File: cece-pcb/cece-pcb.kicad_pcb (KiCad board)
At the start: 2 copper layers, 64 x 90 mm, 52 parts, among them J1 SERIAL, J2 HTU21D, J3 Li-Ion Battery, J4 VAC, K1 SANYOU_SRD_Form_C, Q1 Q_NPN, Q2 Q_NPN, SW1 RES, U1 ESP-12F, U2 MCP73811T-420I-OT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

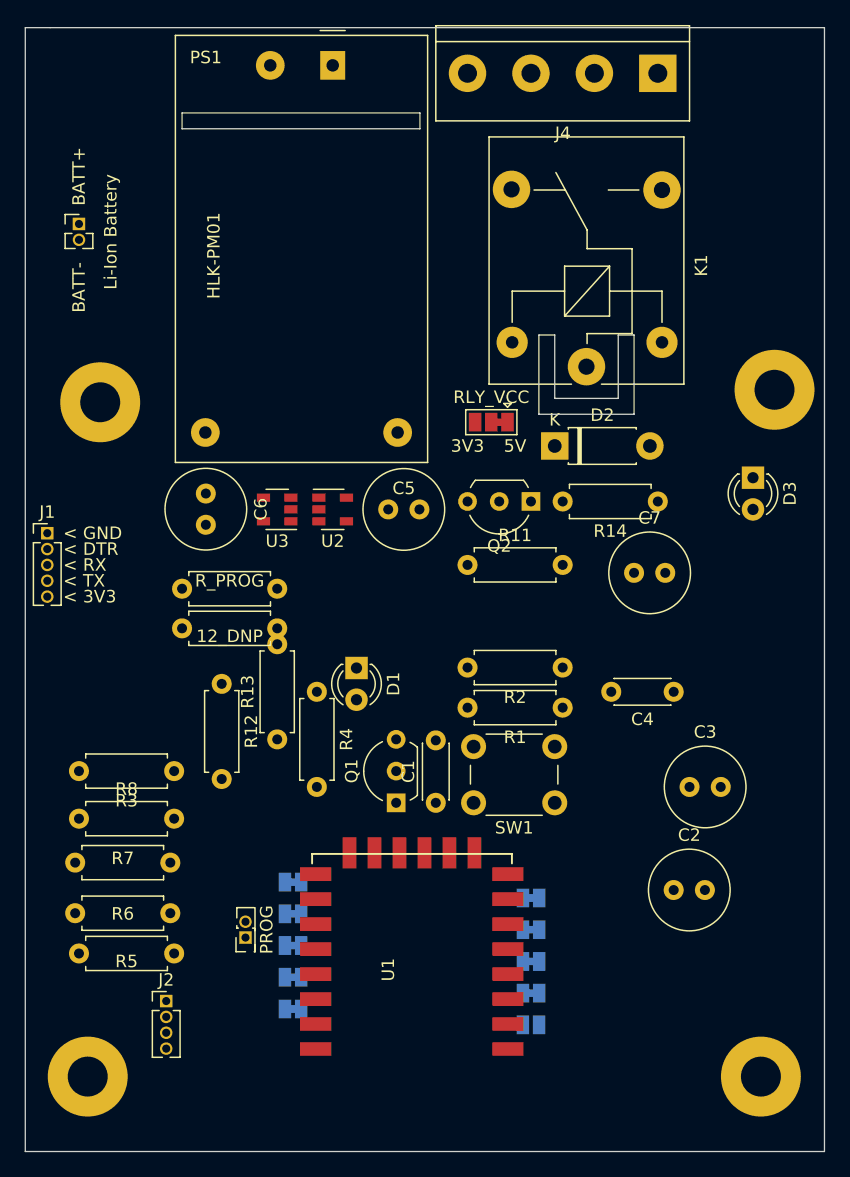
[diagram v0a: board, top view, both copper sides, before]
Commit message: Complete ESP-12 part of the PCB
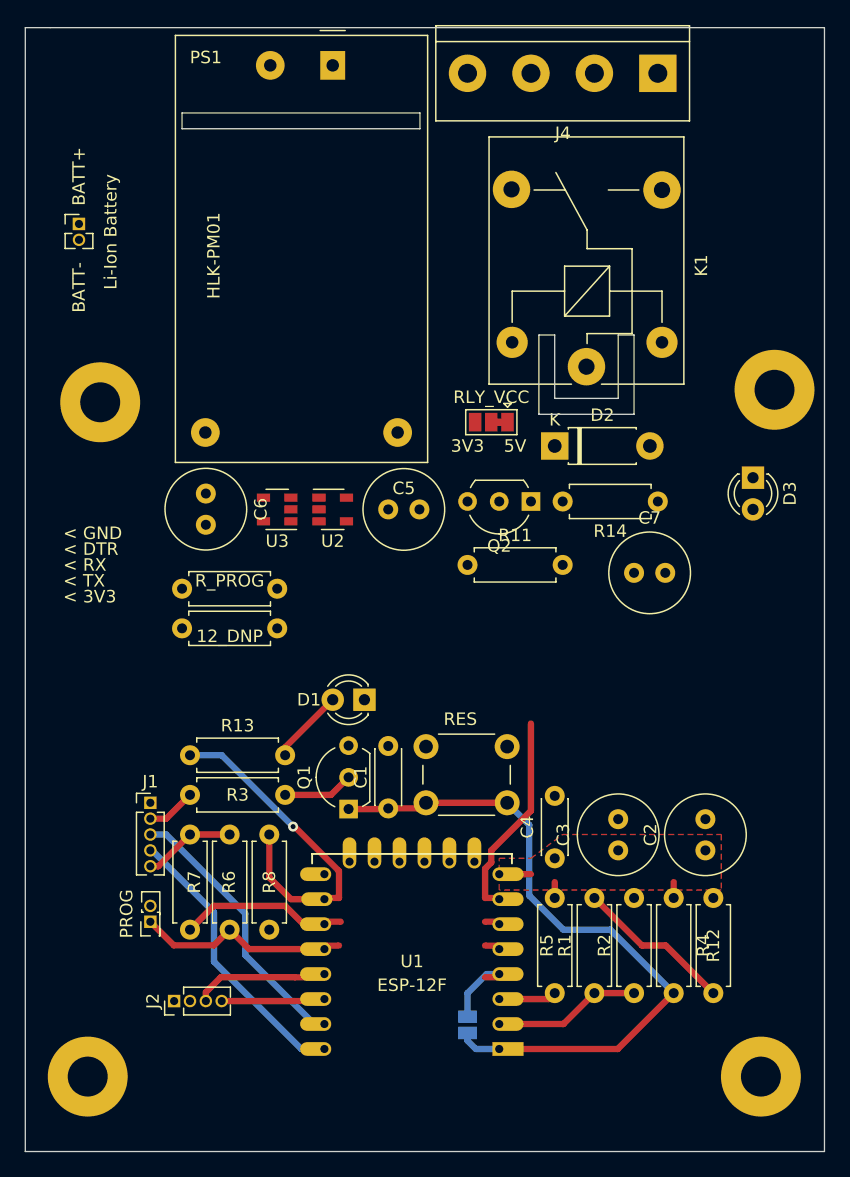
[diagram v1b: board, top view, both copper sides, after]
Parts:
- removed JP10: D4/GPIO2, Jumper:SolderJumper-2_P1.3mm_Bridged_Pad1.0x1.5mm
- removed JP2: D0/GPIO16, Jumper:SolderJumper-2_P1.3mm_Bridged_Pad1.0x1.5mm
- removed JP3: D5/GPIO14, Jumper:SolderJumper-2_P1.3mm_Bridged_Pad1.0x1.5mm
- removed JP4: D6/GPIO12, Jumper:SolderJumper-2_P1.3mm_Bridged_Pad1.0x1.5mm
- removed JP5: D7/GPIO13, Jumper:SolderJumper-2_P1.3mm_Bridged_Pad1.0x1.5mm
- removed JP6: D8/GPIO15, Jumper:SolderJumper-2_P1.3mm_Bridged_Pad1.0x1.5mm
- removed JP7: D1/GPIO5, Jumper:SolderJumper-2_P1.3mm_Bridged_Pad1.0x1.5mm
- removed JP8: D2/GPIO4, Jumper:SolderJumper-2_P1.3mm_Bridged_Pad1.0x1.5mm
- removed JP9: D3/GPIO0, Jumper:SolderJumper-2_P1.3mm_Bridged_Pad1.0x1.5mm
- added NT1: D0/GPIO16, NetTie:NetTie-2_SMD_Pad0.5mm, F.Cu at (147.3, 106.0)
- added NT2: D5/GPIO14, NetTie:NetTie-2_SMD_Pad0.5mm, F.Cu at (147.3, 103.5)
- added NT3: D6/GPIO12, NetTie:NetTie-2_SMD_Pad0.5mm, F.Cu at (147.3, 101.6)
- added NT4: D7/GPIO13, NetTie:NetTie-2_SMD_Pad0.5mm, F.Cu at (147.3, 99.7)
- added NT5: D8/GPIO15, NetTie:NetTie-2_SMD_Pad0.5mm, F.Cu at (134.6, 99.7)
- added NT6: D1/GPIO5, NetTie:NetTie-2_SMD_Pad0.5mm, F.Cu at (132.1, 108.0)
- added NT7: D2/GPIO4, NetTie:NetTie-2_SMD_Pad0.5mm, F.Cu at (132.1, 106.0)
- added NT8: D3/GPIO0, NetTie:NetTie-2_SMD_Pad0.5mm, F.Cu at (134.6, 103.5)
- added NT9: D4/GPIO2, NetTie:NetTie-2_SMD_Pad0.5mm, F.Cu at (134.8, 101.6)
- U1: footprint ESP8266:ESP-12E_SMD -> ESP8266:ESP-12E
- moved R12 46.5 mm to (165.1, 107.3), turned to 90 degrees
- moved R4 33.0 mm to (161.9, 99.7)
- moved R5 30.6 mm to (152.4, 107.3), turned to 90 degrees
- moved R2 26.7 mm to (158.8, 107.3), turned to 90 degrees
- moved J1 23.1 mm to (120.0, 92.1)
- moved R1 23.0 mm to (155.6, 107.3), turned to 90 degrees
- moved R8 17.6 mm to (129.5, 102.2), turned to 90 degrees
- moved C4 16.4 mm to (152.4, 96.5), turned to 90 degrees
- moved R3 9.09 mm to (130.8, 91.4)
- moved JP11 7.73 mm to (120.0, 101.6)
- moved C3 7.65 mm to (157.5, 95.9), turned to 90 degrees
- moved R13 7.10 mm to (123.2, 88.3), turned to 0 degrees
- moved R7 5.60 mm to (123.2, 102.2), turned to 90 degrees
- moved JP1 5.08 mm to (145.4, 109.9), turned to 90 degrees
- moved R6 4.93 mm to (126.4, 102.2), turned to 90 degrees
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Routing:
- net /ESP-12_common/RST: track 0.00 -> 55.1 mm
- net /TX: track 0.00 -> 22.8 mm
- net /RX: track 0.00 -> 22.2 mm
- net /ESP-12_common/D8: track 0.00 -> 18.0 mm, vias 0 -> 1
- net /ESP-12_common/GPIO0: track 0.00 -> 17.5 mm
- net /RLY: track 0.00 -> 15.5 mm
- net /ESP-12_common/A0: track 0.00 -> 12.7 mm
- net +3V3: track 0.00 -> 12.5 mm
- net /ESP-12_common/GPIO2: track 0.00 -> 12.2 mm
- net /ESP-12_common/ADC: track 0.00 -> 11.8 mm
- net /ESP-12_common/GPIO15: track 0.00 -> 10.2 mm
- net /HTU_SDA: track 0.00 -> 8.32 mm
- net Net-(D1-Pad2): track 0.00 -> 6.02 mm
- net /HTU_SCL: track 0.00 -> 5.82 mm
- net Net-(Q1-Pad2): track 0.00 -> 5.66 mm
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- added copper zone on F.Cu, net +3V3

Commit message: Finish first board revision
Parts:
- removed JP12: RLY_VCC, Jumper:SolderJumper-3_P1.3mm_Bridged12_Pad1.0x1.5mm
- removed R12: 100k, Resistor_THT:R_Axial_DIN0207_L6.3mm_D2.5mm_P7.62mm_Horizontal
- added JP2: VBATT_A0, Jumper:SolderJumper-2_P1.3mm_Bridged_Pad1.0x1.5mm, F.Cu at (161.8, 94.1)
- D3: footprint LED_THT:LED_D3.0mm -> LED_THT:LED_D5.0mm
- U2: moved to B.Cu
- moved J3 43.5 mm to (135.9, 83.5), turned to 270 degrees
- moved U3 25.6 mm to (150.4, 84.3), turned to 270 degrees
- moved C6 16.6 mm to (140.2, 72.6), turned to 180 degrees
- moved C5 15.6 mm to (124.0, 72.6)
- moved C7 15.4 mm to (146.1, 65.0), turned to 270 degrees
- moved C2 13.5 mm to (155.7, 85.6), turned to 0 degrees
- moved D3 12.1 mm to (161.0, 75.7), turned to 90 degrees
- moved R10 11.4 mm to (133.6, 77.7), turned to 90 degrees
- moved R11 9.71 mm to (154.2, 77.2), turned to 180 degrees
- moved H3 9.43 mm to (165.0, 67.0)
- moved D1 8.90 mm to (128.3, 84.3)
- moved H4 8.86 mm to (161.0, 110.0)
- moved J2 8.12 mm to (129.5, 105.2), turned to 0 degrees
- moved H2 8.06 mm to (122.0, 110.0)
- moved R9 8.01 mm to (130.6, 70.1), turned to 270 degrees
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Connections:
- C7 pad 1: Net-(C7-Pad1) -> +BATT
- D2 pad 1: Net-(C7-Pad1) -> +BATT
- J4 pad 1: /NC -> /NO
- J4 pad 2: /NO -> /NC
- K1 pad 5: Net-(C7-Pad1) -> +BATT
- NT1 pad 1: (no net) -> /ESP-12_common/D0
- NT2 pad 1: (no net) -> /ESP-12_common/D5|SCK
- NT3 pad 1: (no net) -> /ESP-12_common/D6|MISO
- NT8 pad 2: (no net) -> /ESP-12_common/D3
- NT9 pad 2: (no net) -> /ESP-12_common/D4
- R14 pad 2: Net-(C7-Pad1) -> +BATT
- U1 pad 17: (no net) -> Net-(U1-Pad17)
- U1 pad 18: (no net) -> Net-(U1-Pad18)
- U1 pad 19: (no net) -> Net-(U1-Pad19)
- U1 pad 20: (no net) -> Net-(U1-Pad20)
- U1 pad 21: (no net) -> Net-(U1-Pad21)
- U1 pad 22: (no net) -> Net-(U1-Pad22)
- U3 pad 4: (no net) -> Net-(U3-Pad4)
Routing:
- net +BATT: track 0.00 -> 82.4 mm
- net +3V3: track 12.5 -> 75.2 mm
- net /C: track 0.00 -> 55.4 mm
- net /RLY: track 15.5 -> 47.6 mm, vias 0 -> 2
- net Net-(D2-Pad2): track 0.00 -> 21.9 mm
- net +5V: track 0.00 -> 20.9 mm
- net /NC: track 0.00 -> 14.6 mm
- net /LN: track 0.00 -> 11.1 mm
- net /ESP-12_common/RST: track 55.1 -> 44.4 mm
- net /NO: track 0.00 -> 9.48 mm
- net /ESP-12_common/A0: track 12.7 -> 4.24 mm
- net Net-(R10-Pad1): track 0.00 -> 6.15 mm
- net /ESP-12_common/D8: track 18.0 -> 12.4 mm, vias 1 -> 2
- net /ESP-12_common/ADC: track 11.8 -> 17.4 mm
- net /HTU_SDA: track 8.32 -> 2.91 mm
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- added copper zone on B.Cu, net GND
- added copper zone on F.Cu, net GND
- removed copper zone on F.Cu, net +3V3
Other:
- board size 64 x 90 mm -> 57 x 86 mm
- board text added: "+"
- board text added: "<"
- board text removed: "3V3"
- board text removed: "5V"
- board text removed: "< 3V3"
- board text removed: "< DTR"
- board text removed: "< GND"
- board text removed: "< RX"
- board text removed: "< TX"
- board text removed: "BATT+"
- board text removed: "BATT-"

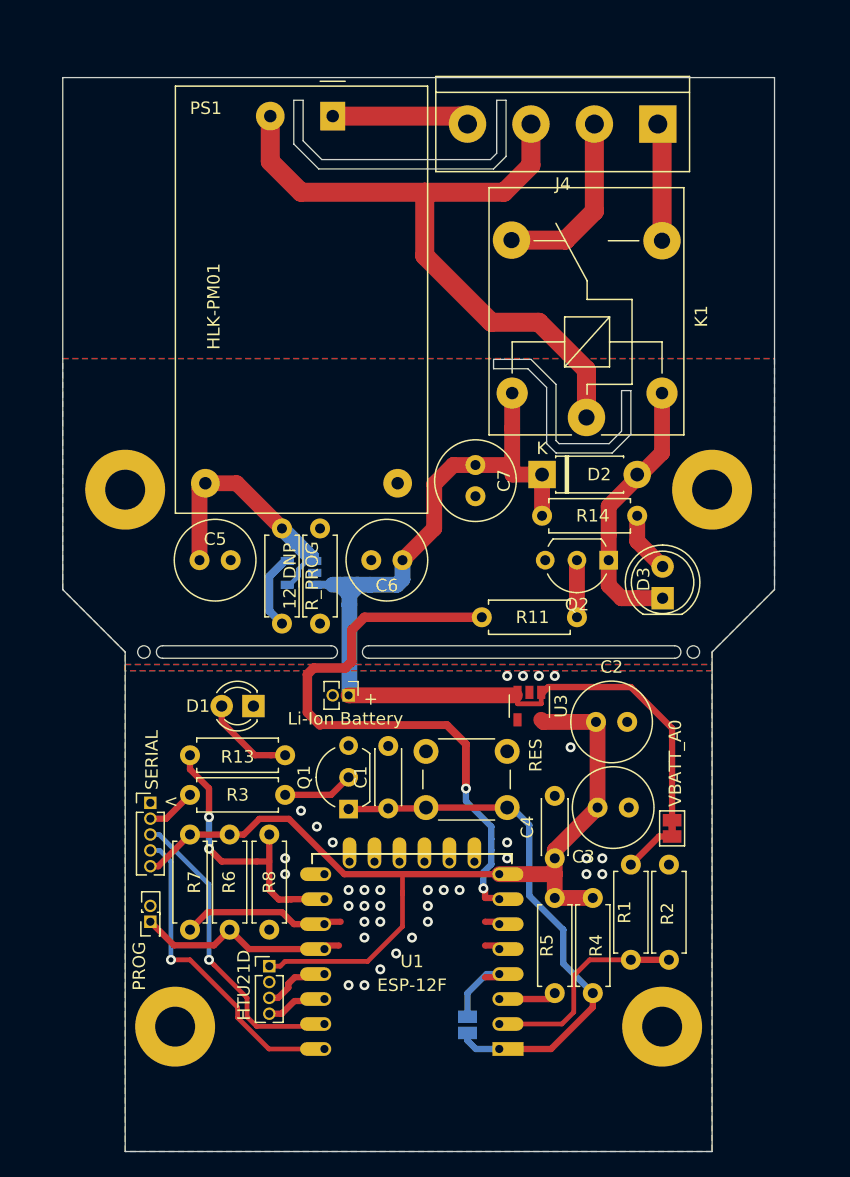
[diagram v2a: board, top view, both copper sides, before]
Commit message: Make board DRC-friendly
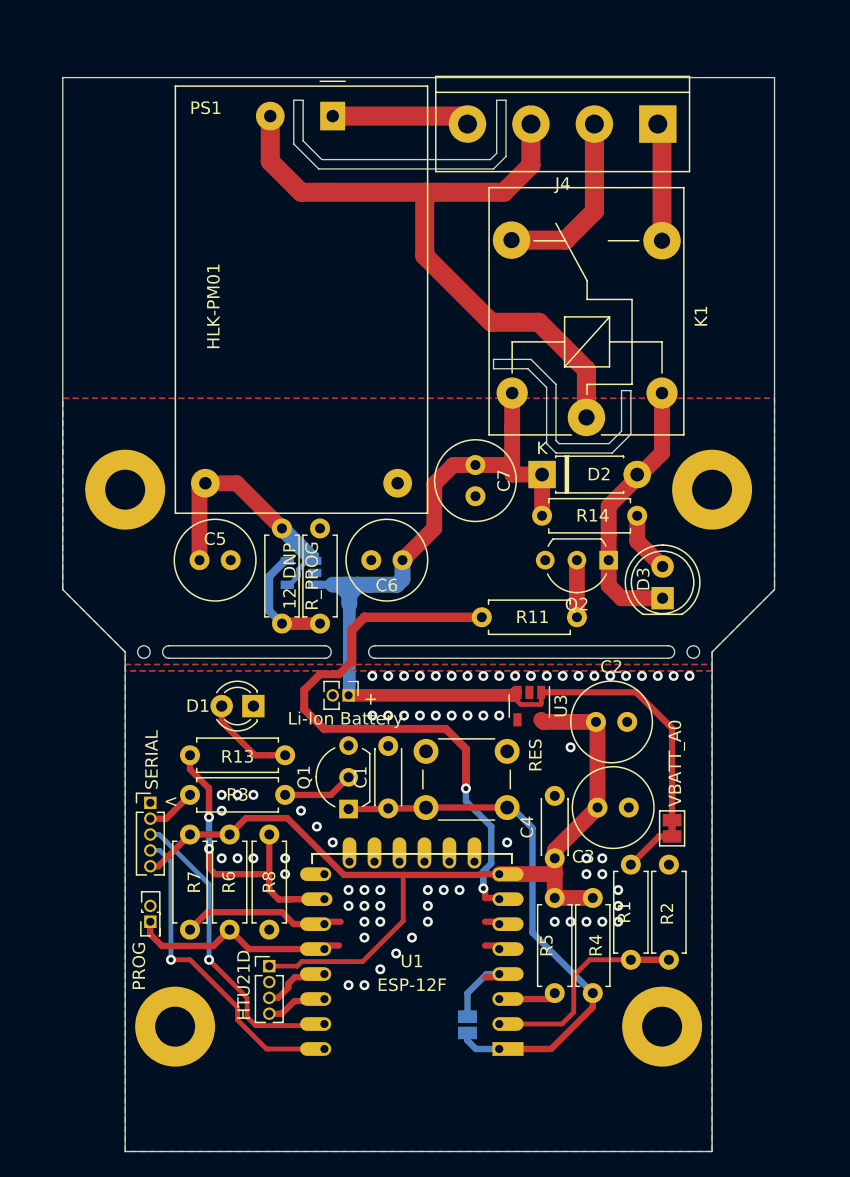
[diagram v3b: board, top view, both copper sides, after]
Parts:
- moved NT5 1.02 mm to (129.0, 97.8)
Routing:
- net Net-(R10-Pad1): track 6.15 -> 9.20 mm
- net /ESP-12_common/D8: track 12.4 -> 13.7 mm
- net /ESP-12_common/GPIO0: track 17.5 -> 18.1 mm
- net /RLY: track 47.6 -> 47.1 mm
- net GND: vias 35 -> 74
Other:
- outline, holes or cut-outs redrawn
- net class Default: clearance 0.2 -> 0.254; trace_width 0.25 -> 0.127
- rule trace_clearance: 0.2 -> 0.254
- rule trace_min: 0.2 -> 0.127
- rule via_min_drill: 0.3 -> 0.2
- rule via_min_size: 0.4 -> 0.45

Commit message: Hang the ESP8266 antenna outside of the board for better RF performance
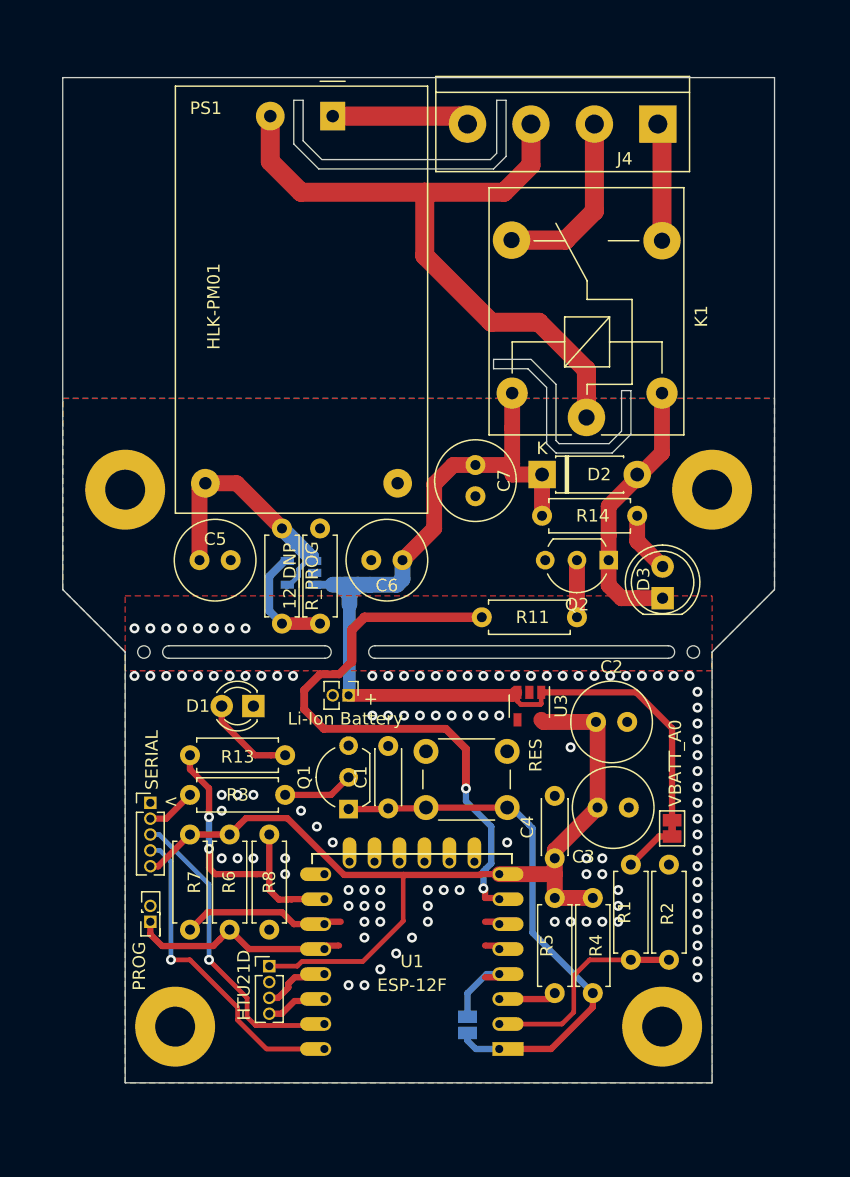
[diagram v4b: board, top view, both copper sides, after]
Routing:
- net GND: vias 74 -> 112
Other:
- board size 57 x 86 mm -> 57 x 80.5 mm
- board text added: "C"
- board text added: "L/N"
- board text added: "NC"
- board text added: "NO"
- board text added: "See also: https://www.espressif.com/sites/default/files/documentation/esp32_hardware_design_guidelines_en.pdf"

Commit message: More touches to the layout. Almost finished
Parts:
- D3: footprint LED_THT:LED_D5.0mm -> LED_THT:LED_D3.0mm
- moved JP11 1.91 mm to (120.0, 103.5), turned to 270 degrees
- moved J1 0.51 mm to (120.0, 91.6)
- moved J2 0.25 mm to (129.8, 105.2)
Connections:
- J1 pad 1: GND -> +3V3
- J1 pad 5: +3V3 -> GND
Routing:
- net /ESP-12_common/GPIO0: track 18.1 -> 16.7 mm
- net /RX: track 25.8 -> 26.6 mm
- net GND: vias 112 -> 150

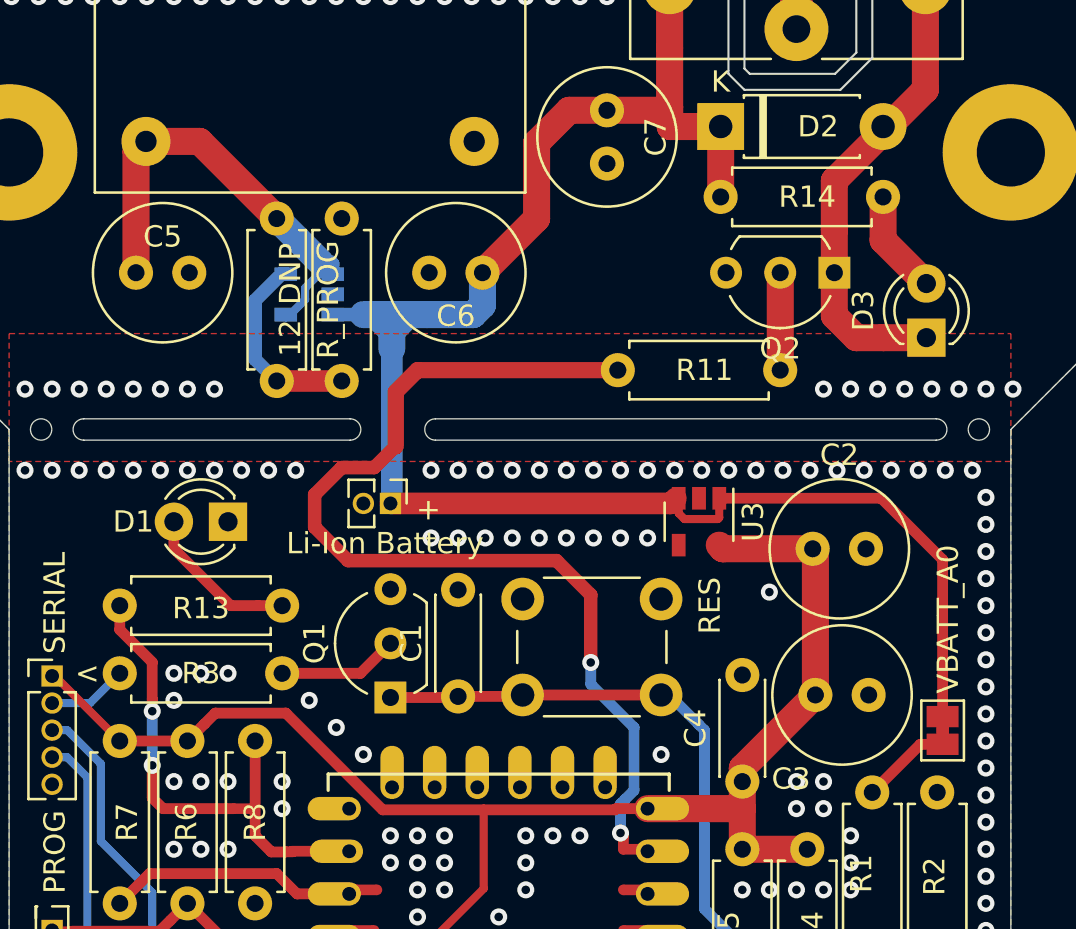
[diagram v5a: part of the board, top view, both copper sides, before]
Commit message: better grounding layout for regulator ICs
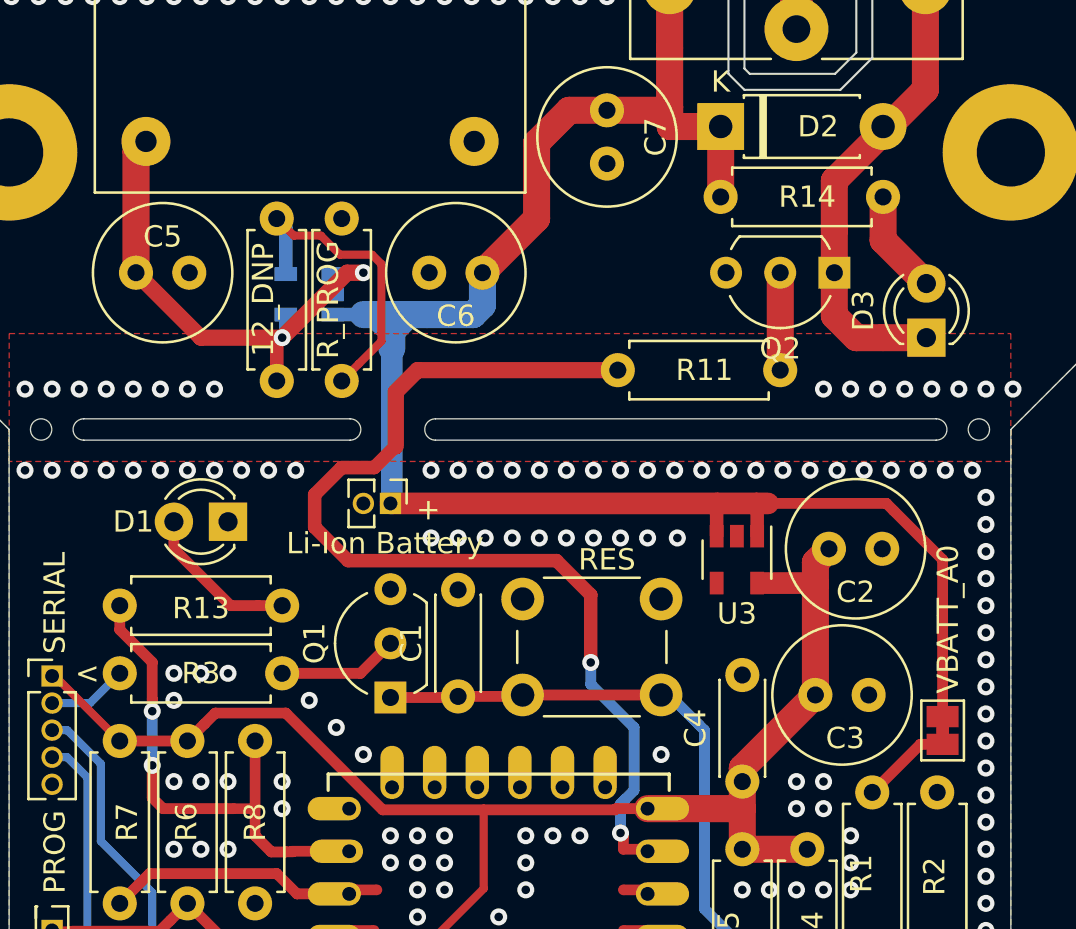
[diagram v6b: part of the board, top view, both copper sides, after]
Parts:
- moved R9 7.62 mm to (130.6, 77.7), turned to 90 degrees
- moved U3 2.51 mm to (152.1, 86.1)
- moved C2 0.76 mm to (156.5, 85.6)
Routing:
- net Net-(R10-Pad1): track 9.20 -> 15.4 mm
- net +5V: track 20.9 -> 24.7 mm, vias 0 -> 2
- net +BATT: track 82.1 -> 84.3 mm
- net +3V3: track 75.1 -> 73.3 mm
